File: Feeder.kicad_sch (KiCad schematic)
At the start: 43 parts, among them J101 Conn_02x03_Odd_Even, J102 Conn_01x03_Pin, U101 XBLW 24C02S(XBLW)

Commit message: First layout complete - DRC not clear yet.
Signed-off-by: Jean Alinei <jean.alinei@owntech.org>
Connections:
- net +12V_DGND: now also J101.5 (Pin_5); no longer J101.1 (Pin_1)
- net +5V_DGND: now also J101.6 (Pin_6); no longer J101.2 (Pin_2)
- net SCL: now also J101.2 (Pin_2); no longer J101.6 (Pin_6)
- net SDA: now also J101.1 (Pin_1); no longer J101.5 (Pin_5)
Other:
- sheet dc-dc_12-6: file dc-dc_12-5.kicad_sch -> dc-dc_12-6.kicad_sch
- note added: "ADDR : Ox50"
- moved on the sheet: C101, C102, C103, C104, C105, C106, C107, C108, C109, C110, C111, C112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

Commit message: updated gitignore and wip on the pcb. modified the functionnal diagram on the schematic
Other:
- note added: "12-120V Bus supply mode"
- note added: "12V_P 0"
- note added: "12V_P 1"
- note added: "DIGITAL"
- note added: "External Power Header"
- note added: "POWER"
- note added: "V_{HIGH}"
- note removed: "12-120V Bus supply"
- note removed: "12V in"
- note removed: "12VP"
- note removed: "12V_P 0 12V_P 1"

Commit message: small tweaks, silkscreen, component placements
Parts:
- R101: Reserved1 0033a278416cfa2b888d35575b40f177dfa85dffb5a098 -> (none)
- R107: LCSC C2906899 -> (none)
- R110, R111: value 1k -> 2k2; LCSC C2906899 -> (none)
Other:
- note added: "I_LED = (12 - Vf) / 2200 For Vf = 2,7 V : I_LED = 9,3 / 2200 = 4,23 mA For Vf = 3,2 V : I_LED = 8,8 / 2200 = 4,00 mA"
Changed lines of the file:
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@@
 		)
 	)
+	(text "I_LED = (12 - Vf) / 2200\n\nFor Vf = 2,7 V :\nI_LED = 9,3 / 2200 = 4,23 mA\n\nFor Vf = 3,2 V :\nI_LED = 8,8 / 2200 = 4,00 mA"
+		(exclude_from_sim no)
+		(at 193.548 198.12 0)
+		(effects
+			(font
+				(size 1.27 1.27)
+			)
+			(justify left)
+		)
+	)
 	(text "isolated"
 		(exclude_from_sim no)
@@
 	(text "     Lights up when \n<-  ~{EN} is LOW\n     (enabled)"
 		(exclude_from_sim no)
-		(at 108.712 207.772 0)
+		(at 110.744 202.184 0)
 		(effects
 			(font
@@
 			)
 		)
-		(property "Reserved1" "0033a278416cfa2b888d35575b40f177dfa85dffb5a098"
+		(property "Reserved1" ""
+			(at 86.36 201.93 0)
+			(hide yes)
+			(show_name no)
+			(do_not_autoplace no)
+			(effects
+				(font
+					(size 1.27 1.27)
+				)
+			)
+		)
+		(property "LCSC" ""
 			(at 86.36 201.93 0)
 			(hide yes)
@@
 			)
 		)
-		(property "Value" "1k"
+		(property "Value" "2k2"
 			(at 182.88 197.866 0)
 			(show_name no)
@@
 			)
 		)
-		(property "LCSC" "C2906899"
+		(property "LCSC" ""
 			(at 179.07 196.85 90)
 			(hide yes)
@@
 			)
 		)
-		(property "Value" "1k"
+		(property "Value" "2k2"
 			(at 161.29 197.866 0)
 			(show_name no)
@@
 			)
 		)
-		(property "LCSC" "C2906899"
+		(property "LCSC" ""
 			(at 157.48 196.85 90)
 			(hide yes)
@@
 			)
 		)
-		(property "LCSC" "C2906899"
+		(property "LCSC" ""
 			(at 102.87 194.31 90)
 			(hide yes)

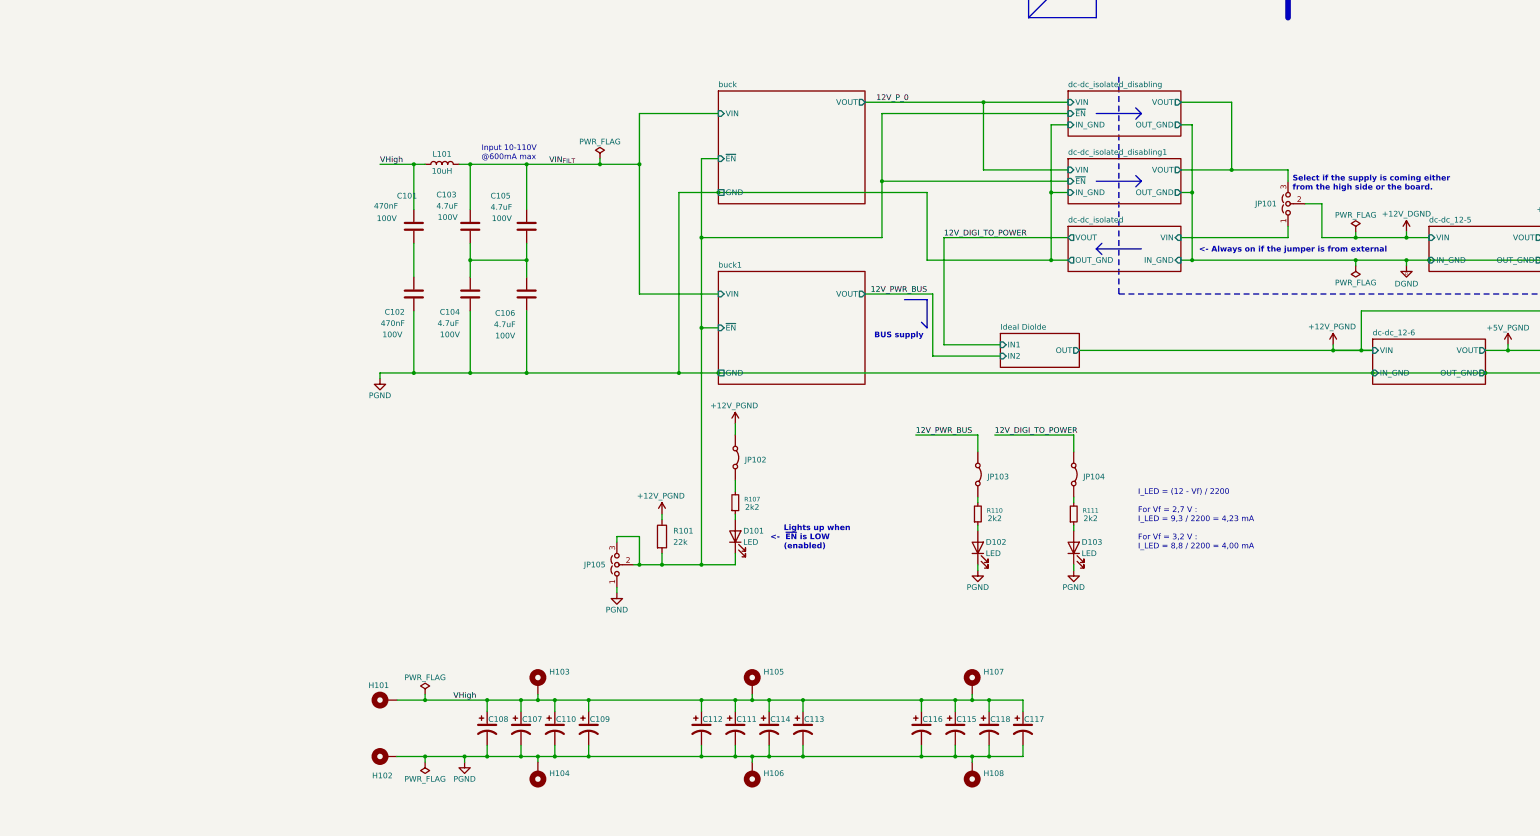
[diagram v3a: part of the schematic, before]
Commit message: added propoer filter and rerouted filters + enhancements all arround the board. no drc errors except soic8 isolation
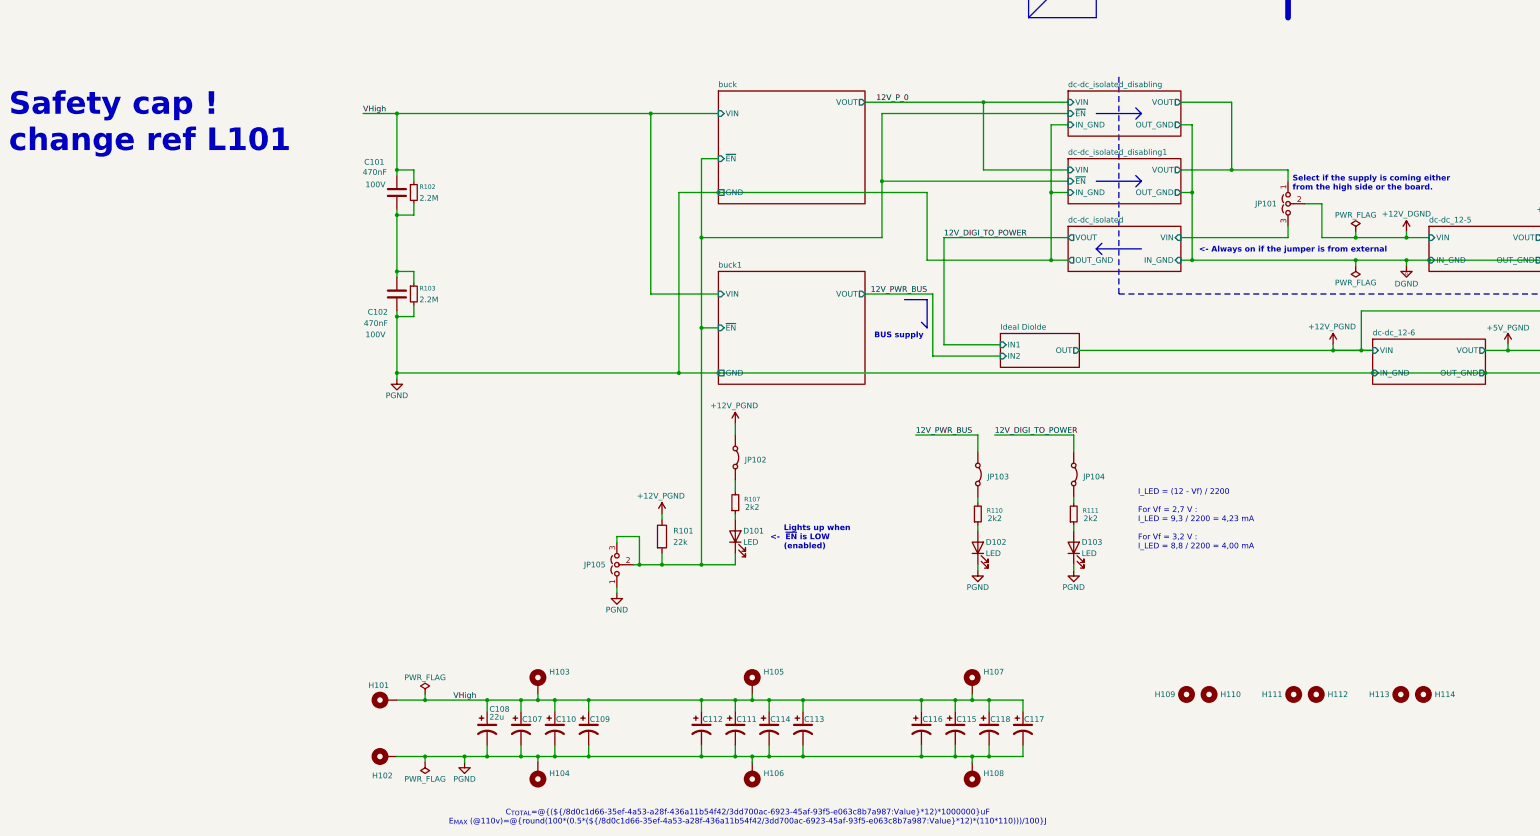
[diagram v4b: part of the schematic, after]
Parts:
- removed C103, C104, C105, C106: 4.7uF, Footprints:C_1210_3225Metric, symbol Device:C
- removed L101: 10uH, Inductor_SMD:L_1210_3225Metric, symbol Device:L
- added H109, H110, H111, H112, H113, H114: MountingHole, Footprints:Hole_signal_bottom_board_lookup, symbol Mechanical:MountingHole
- added R102, R103: 2.2M, Resistor_SMD:R_0603_1608Metric, symbol Device:R_Small
- C107, C108, C109, C110, C111, C112, C113, C114, C115, C116, C117, C118: value C_Polarized_US -> 22u
- J102: footprint (none) -> Connector_PinHeader_2.54mm:PinHeader_1x03_P2.54mm_Vertical
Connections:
- net PGND: now also R103.2
- net VHigh: now also R102.1
- net dc-dc_isolated/VIN: now also JP101.3 (B); no longer JP101.1 (A)
- net dc-dc_isolated_disabling/VOUT: now also JP101.1 (A); no longer JP101.3 (B)
- net at C101.2, C102.1: now also R102.2, R103.1
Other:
- note added: "C_{TOTAL}=@{(${/8d0c1d66-35ef-4a53-a28f-436a11b54f42/3dd700ac-6923-45af-93f5-e063c8b7a987:Value}*12)*1000000}uF E_{MAX} (@110v)=@{round(100*(0.5*(${/8d0c1d66-35ef-4a53-a28f-436a11b54f42/3dd700ac-6923-45af-93f5-e063c8b7a987:Value}*12)*(110*110)))/100}J"
- note added: "Safety cap ! change ref L101"
- note removed: "Input 10-110V @600mA max"
- moved on the sheet: C101, C102

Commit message: added y cap and changed the inductor value, added simulator of pi filter
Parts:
- added C103: 470p, Footprints:SAFETY_CAP_8.1x6mm, symbol Device:C
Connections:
- net DGND: now also C103.2
- net PGND: now also C103.1
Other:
- note added: "Safety CAP"
- note removed: "Safety cap ! change ref L101"

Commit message: Found IC for ORing function. Added all LCSC refs. Found proper header stackup.
Signed-off-by: Jean Alinei <jean.alinei@owntech.org>
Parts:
- added U102: MX5050S3028A2, Package_SO:SOIC-8_3.9x4.9mm_P1.27mm, symbol Symbols:MX5050
- C101, C102: LCSC (none) -> C596323; Reserved1 541c32eba89ffcf7615ab170cc4034ba7c4f621972be10 -> (none); Voltage 100V -> (none); manf# GRM21BR72A474KA73L -> (none)
- C107, C108, C109, C110, C111, C112, C113, C114, C115, C116, C117, C118: LCSC (none) -> C487461
- C119: LCSC (none) -> C14663
- J101: value Conn_02x03_Odd_Even -> (none); footprint Connector_PinHeader_2.54mm:PinHeader_2x03_P2.54mm_Vertical -> Footprints:PinHeader_2x03_P2.54mm_Vertical; LCSC (none) -> C49056253
- J102: value Conn_01x03_Pin -> (none); footprint Connector_PinHeader_2.54mm:PinHeader_1x03_P2.54mm_Vertical -> Footprints:PinHeader_1x03_P2.54mm_Vertical; LCSC (none) -> C46971097
- R101: value 22k -> 10K; footprint Footprints:R_0805_2012Metric -> Resistor_SMD:R_0603_1608Metric; LCSC (none) -> C25804; Package 0805 -> (none); manf# CR0805-FX-1003ELF -> (none)
- R102, R103: LCSC (none) -> C22356574
- R107, R110, R111: LCSC (none) -> C25879; Tolerance 1% -> (none)
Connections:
- net +12V_PGND: now also U102.5 (OUT2), U102.6 (OUT2), U102.7 (OUT1), U102.8 (OUT1)
- net 12V_DIGI_TO_POWER: now also U102.1 (IN1)
- net 12V_PWR_BUS: now also U102.3 (IN2)
- net PGND: now also U102.2 (GND1), U102.4 (GND2)
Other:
- removed sheet Ideal Diolde
- moved on the sheet: C101, C102, C103, C107, C108, C109, C110, C111, C112, C113, C114, C115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

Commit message: Reworked the schematic & removed deprecated datasheets.
Signed-off-by: Jean Alinei <jean.alinei@owntech.org>
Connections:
- net buck/~{EN} renamed ~{EN}
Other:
- note added: "ADDR : 0x50"
- note added: "JP105 sets ~{EN} LOW (enabled)."
- note added: "Lights up when ~{EN} is LOW (enabled)"
- note added: "Mechanical openings for probing cables coming from power modules."
- note added: "Output power rails."
- note added: "Select if the supply is coming either from the high side or from DGND side from the external power connectors. If coming from external connectors set ~{EN} to HIGH (disable) on JP105"
- note removed: "ADDR : Ox50"
- note removed: "Lights up when <- ~{EN} is LOW (enabled)"
- note removed: "Select if the supply is coming either from the high side or the board."
- moved on the sheet: C101, C102, C103, C107, C108, C109, C110, C111, C112, C113, C114, C115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

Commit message: Added datasheets & updated components descriptions & values
Signed-off-by: Jean Alinei <jean.alinei@owntech.org>
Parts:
- D101, D102, D103: value LED -> CT-1005UBC-P4
- J101: value (none) -> PZ254V-22-06-A60-1500
- J102: value (none) -> PZ254V-21-03-A60-1500
- U101: value XBLW 24C02S(XBLW) -> 24C02S(XBLW)
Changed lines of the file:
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@@
 			)
 		)
-		(property "Description" "Resistor"
+		(property "Description" "10kΩ ±1% 100mW 0603 Thick Film Resistor"
 			(at 80.01 208.28 0)
 			(hide yes)
@@
 			)
 		)
-		(property "Description" "Dual 4A ideal-diode ORing, integrated MOSFET"
+		(property "Description" "28mΩ 2 SOP-8L OR Controllers, Ideal Diodes"
 			(at 144.78 161.29 0)
 			(hide yes)
@@
 			)
 		)
-		(property "Description" "Polarized capacitor, US symbol"
+		(property "Description" "22uF ±20% 160V Aluminum Electrolytic Capacitors 10000hrs@105℃"
 			(at 158.75 259.08 0)
 			(hide yes)
@@
 			)
 		)
-		(property "Description" "Polarized capacitor, US symbol"
+		(property "Description" "22uF ±20% 160V Aluminum Electrolytic Capacitors 10000hrs@105℃"
 			(at 166.37 259.08 0)
 			(hide yes)
@@
 			)
 		)
-		(property "Description" "Y Safety capacitor"
+		(property "Description" "470pF ±10% 500V Safety Capacitor Y1 SMD,8.1x6mm"
 			(at 264.16 147.32 0)
 			(hide yes)
@@
 			)
 		)
-		(property "Description" "Polarized capacitor, US symbol"
+		(property "Description" "22uF ±20% 160V Aluminum Electrolytic Capacitors 10000hrs@105℃"
 			(at 151.13 259.08 0)
 			(hide yes)
@@
 			)
 		)
-		(property "Description" "Resistor, small symbol"
+		(property "Description" "-55℃~+155℃ 100mW 2.2MΩ 75V Thick Film Resistor ±200ppm/℃ ±5% 0603 Chip Resistor - Surface Mount RoHS"
 			(at 55.88 154.94 0)
 			(hide yes)
@@
 			)
 		)
-		(property "Description" "Polarized capacitor, US symbol"
+		(property "Description" "22uF ±20% 160V Aluminum Electrolytic Capacitors 10000hrs@105℃"
 			(at 271.78 259.08 0)
 			(hide yes)
@@
 			)
 		)
-		(property "Value" "LED"
+		(property "Value" "CT-1005UBC-P4"
 			(at 61.722 217.17 90)
 			(show_name no)
@@
 			)
 		)
-		(property "Description" "Light emitting diode"
+		(property "Description" "120° 30mcd~70mcd Blue 5mA 2.7V~3.1V 0.8mm x 0.5mm square LED 462.5nm~470nm 0402 LED Indication - Discrete"
 			(at 63.5 215.9 0)
 			(hide yes)
@@
 			)
 		)
-		(property "Value" ""
+		(property "Value" "PZ254V-21-03-A60-1500"
 			(at 266.7 200.6601 0)
 			(hide yes)
@@
 			)
 		)
-		(property "Description" "Generic connector, single row, 01x03, script generated"
+		(property "Description" "Through Hole 1 2.54mm Square pin 3A 6mm 6mm 3P -40℃~+105℃ 3mm Black 1x3P Through Hole,P=2.54mm Headers, Male Pins RoHS"
 			(at 265.43 201.93 0)
 			(hide yes)
@@
 			)
 		)
-		(property "Description" "Unpolarized capacitor"
+		(property "Description" "470nF ±10% 100V Ceramic Capacitor X7R 0805"
 			(at 52.07 154.94 0)
 			(hide yes)
@@
 			)
 		)
-		(property "Description" "Polarized capacitor, US symbol"
+		(property "Description" "22uF ±20% 160V Aluminum Electrolytic Capacitors 10000hrs@105℃"
 			(at 207.01 259.08 0)
 			(hide yes)
@@
 			)
 		)
-		(property "Description" "Polarized capacitor, US symbol"
+		(property "Description" "22uF ±20% 160V Aluminum Electrolytic Capacitors 10000hrs@105℃"
 			(at 256.54 259.08 0)
 			(hide yes)
@@
 			)
 		)
-		(property "Value" "LED"
+		(property "Value" "CT-1005UBC-P4"
 			(at 126.238 220.98 90)
 			(show_name no)
@@
 			)
 		)
-		(property "Description" "Light emitting diode"
+		(property "Description" "120° 30mcd~70mcd Blue 5mA 2.7V~3.1V 0.8mm x 0.5mm square LED 462.5nm~470nm 0402 LED Indication - Discrete"
 			(at 124.46 219.71 0)
 			(hide yes)
@@
 			)
 		)
-		(property "Description" "Resistor, small symbol"
+		(property "Description" "-55℃~+155℃ 100mW 2.2MΩ 75V Thick Film Resistor ±200ppm/℃ ±5% 0603 Chip Resistor - Surface Mount RoHS"
 			(at 55.88 121.92 0)
 			(hide yes)
@@
 			)
 		)
-		(property "Description" "Resistor, small symbol"
+		(property "Description" "2.2kΩ ±1% 62.5mW 0402 Thick Film Resistor"
 			(at 146.05 209.55 0)
 			(hide yes)
@@
 			)
 		)
-		(property "Value" "XBLW 24C02S(XBLW)"
+		(property "Value" "24C02S(XBLW)"
 			(at 281.178 112.522 0)
 			(show_name no)
@@
 			)
 		)
-		(property "Description" "I2C Serial EEPROM, 2Kb (256x8) with Unique Serial Number, SOT-23-5"
+		(property "Description" "2Kbit 1MHz I2C SOT23-5 Memory RoHS"
 			(at 303.53 124.46 0)
 			(hide yes)
@@
 			)
 		)
-		(property "Description" "Polarized capacitor, US symbol"
+		(property "Description" "22uF ±20% 160V Aluminum Electrolytic Capacitors 10000hrs@105℃"
 			(at 199.39 259.08 0)
 			(hide yes)
@@
 			)
 		)
-		(property "Description" "Polarized capacitor, US symbol"
+		(property "Description" "22uF ±20% 160V Aluminum Electrolytic Capacitors 10000hrs@105℃"
 			(at 173.99 259.08 0)
 			(hide yes)
@@
 			)
 		)
-		(property "Description" "Resistor, small symbol"
+		(property "Description" "2.2kΩ ±1% 62.5mW 0402 Thick Film Resistor"
 			(at 124.46 209.55 0)
 			(hide yes)
@@
 			)
 		)
-		(property "Value" "LED"
+		(property "Value" "CT-1005UBC-P4"
 			(at 147.828 220.98 90)
 			(show_name no)
@@
 			)
 		)
-		(property "Description" "Light emitting diode"
+		(property "Description" "120° 30mcd~70mcd Blue 5mA 2.7V~3.1V 0.8mm x 0.5mm square LED 462.5nm~470nm 0402 LED Indication - Discrete"
 			(at 146.05 219.71 0)
 			(hide yes)
@@
 			)
 		)
-		(property "Description" "Unpolarized capacitor"
+		(property "Description" "470nF ±10% 100V Ceramic Capacitor X7R 0805"
 			(at 52.07 121.92 0)
 			(hide yes)
@@
 			)
 		)
-		(property "Value" ""
+		(property "Value" "PZ254V-22-06-A60-1500"
 			(at 358.14 113.03 0)
 			(hide yes)
@@
 			)
 		)
-		(property "Description" "Generic connector, double row, 02x03, odd/even pin numbering scheme (row 1 odd numbers, row 2 even numbers), script generated (kicad-library-utils/schlib/autogen/connector/)"
+		(property "Description" "Through Hole 2 2.54mm Square pin 3A 3mm 6mm 6P -40℃~+105℃ 6mm Black 2x3P 2.54mm Through Hole,P=2.54mm Headers, Male Pins RoHS"
 			(at 359.41 119.38 0)
 			(hide yes)
@@
 			)
 		)
-		(property "Description" "Polarized capacitor, US symbol"
+		(property "Description" "22uF ±20% 160V Aluminum Electrolytic Capacitors 10000hrs@105℃"
 			(at 248.92 259.08 0)
 			(hide yes)
@@
 			)
 		)
-		(property "Description" "Resistor, small symbol"
+		(property "Description" "2.2kΩ ±1% 62.5mW 0402 Thick Film Resistor"
 			(at 63.5 208.28 0)
 			(hide yes)
@@
 			)
 		)
-		(property "Description" "Polarized capacitor, US symbol"
+		(property "Description" "22uF ±20% 160V Aluminum Electrolytic Capacitors 10000hrs@105℃"
 			(at 222.25 259.08 0)
 			(hide yes)
@@
 			)
 		)
-		(property "Description" "Unpolarized capacitor, small symbol"
+		(property "Description" "100nF ±10% 50V Ceramic Capacitor X7R 0603"
 			(at 314.96 123.19 0)
 			(hide yes)
@@
 			)
 		)
-		(property "Description" "Polarized capacitor, US symbol"
+		(property "Description" "22uF ±20% 160V Aluminum Electrolytic Capacitors 10000hrs@105℃"
 			(at 214.63 259.08 0)
 			(hide yes)
@@
 			)
 		)
-		(property "Description" "Polarized capacitor, US symbol"
+		(property "Description" "22uF ±20% 160V Aluminum Electrolytic Capacitors 10000hrs@105℃"
 			(at 264.16 259.08 0)
 			(hide yes)
